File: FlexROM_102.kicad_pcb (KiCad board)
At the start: 2 copper layers, 16.5 x 34.3 mm, 7 parts, among them J1 27C256 DIP LEGS, U1 28C256

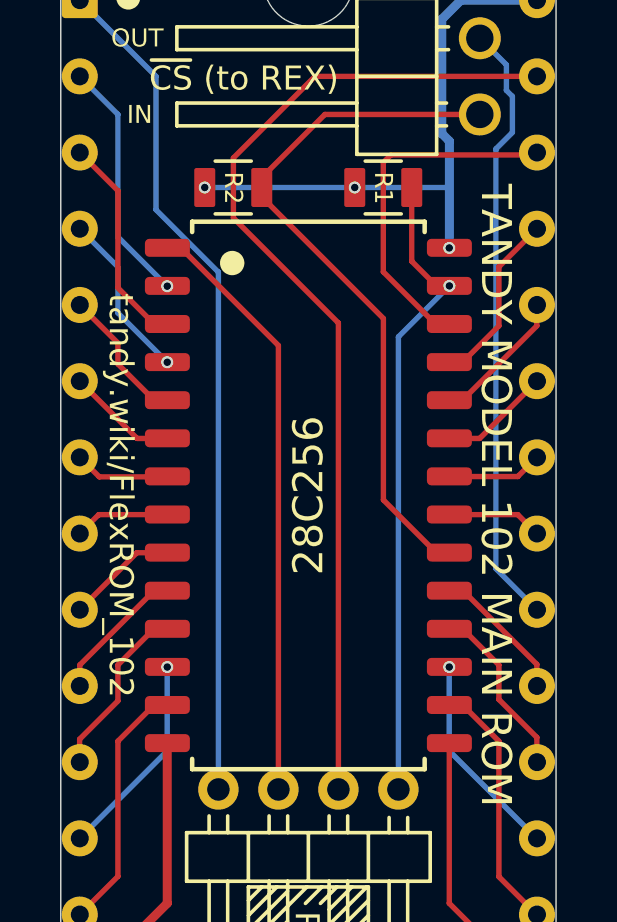
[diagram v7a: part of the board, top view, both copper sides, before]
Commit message: add FlashROM_100_tsop
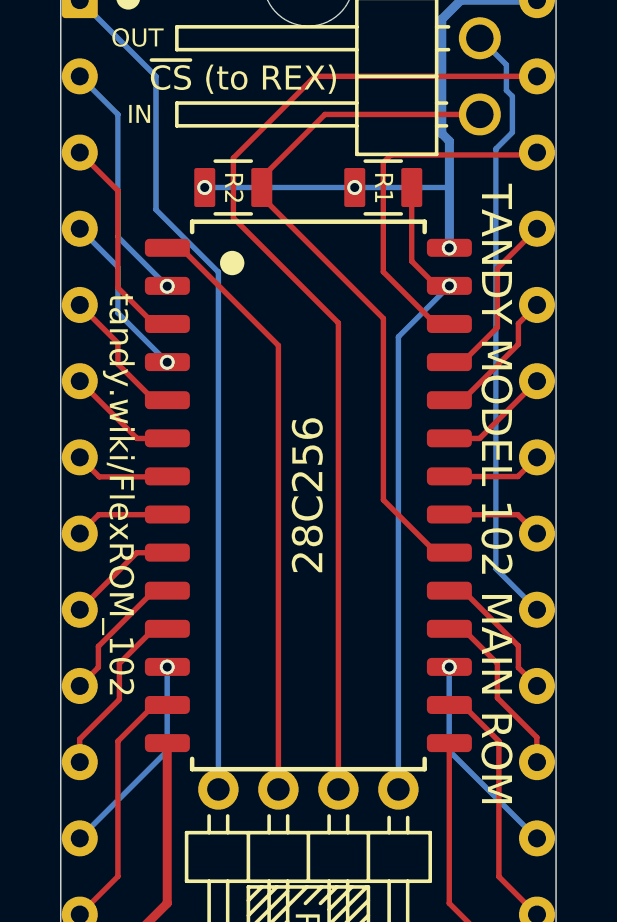
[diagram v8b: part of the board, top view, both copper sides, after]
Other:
- net class Default: via_dia 0.4 -> 0.5; via_drill 0.25 -> 0.3
- rule via_min_drill: 0.25 -> 0.3
- rule via_min_size: 0.4 -> 0.5
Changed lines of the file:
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@@
-(kicad_pcb (version 20171130) (host pcbnew 5.1.8-db9833491~88~ubuntu20.10.1)
+(kicad_pcb (version 20171130) (host pcbnew 5.1.9-73d0e3b20d~88~ubuntu20.10.1)
   (general
     (thickness 1.6)
     (drawings 59)
-    (tracks 134)
+    (tracks 137)
     (zones 0)
     (modules 7)
@@
     (zone_45_only no)
     (trace_min 0.16)
-    (via_size 0.4)
-    (via_drill 0.25)
-    (via_min_size 0.4)
-    (via_min_drill 0.25)
-    (uvia_size 0.4)
-    (uvia_drill 0.25)
+    (via_size 0.5)
+    (via_drill 0.3)
+    (via_min_size 0.5)
+    (via_min_drill 0.3)
+    (uvia_size 0.5)
+    (uvia_drill 0.3)
     (uvias_allowed no)
-    (uvia_min_size 0.4)
-    (uvia_min_drill 0.25)
+    (uvia_min_size 0.5)
+    (uvia_min_drill 0.3)
     (edge_width 0.05)
     (segment_width 0.2)
@@
     (pad_drill 2)
     (pad_to_mask_clearance 0)
+    (solder_mask_min_width 0.22)
     (aux_axis_origin 0 0)
     (grid_origin 127 101.6)
@@
     (clearance 0.16)
     (trace_width 0.18)
-    (via_dia 0.4)
-    (via_drill 0.25)
-    (uvia_dia 0.4)
-    (uvia_drill 0.25)
+    (via_dia 0.5)
+    (via_drill 0.3)
+    (uvia_dia 0.5)
+    (uvia_drill 0.3)
     (add_net /A0)
     (add_net /A1)
@@
     (add_net /~OE)
     (add_net /~WE)
-  )
-  (module 000_LOCAL:NPTH_3mm (layer F.Cu)
-    (at 127 84.455)
-    (fp_text reference REF** (at 0 2.54) (layer F.SilkS) hide
-      (effects (font (size 1.27 1.27) (thickness 0.127)))
-    )
-    (fp_text value NPTH_3mm (at 0 -2.54) (layer F.Fab)
-      (effects (font (size 1.27 1.27) (thickness 0.0127)))
-    )
-    (pad "" np_thru_hole circle (at 0 0) (size 3 3) (drill 3) (layers *.Cu *.Mask))
   )
   (module 000_LOCAL:DIP28_0.6_pcb_sil_pins (layer F.Cu)
@@
       (rotate (xyz 0 0 0))
     )
+  )
+  (module 000_LOCAL:NPTH_3mm (layer F.Cu)
+    (at 127 84.455)
+    (fp_text reference REF** (at 0 2.54) (layer F.SilkS) hide
+      (effects (font (size 1.27 1.27) (thickness 0.127)))
+    )
+    (fp_text value NPTH_3mm (at 0 -2.54) (layer F.Fab)
+      (effects (font (size 1.27 1.27) (thickness 0.0127)))
+    )
+    (pad "" np_thru_hole circle (at 0 0) (size 3 3) (drill 3) (layers *.Cu *.Mask))
   )
   (module 000_LOCAL:PinHeader_1x04_P2.00mm_Horizontal (layer F.Cu)
@@
   (segment (start 131.695 115.195) (end 131.695 109.86) (width 0.18) (layer F.Cu) (net 1))
   (segment (start 134.615 118.115) (end 131.695 115.195) (width 0.18) (layer F.Cu) (net 1))
-  (via (at 122.295 94.625) (size 0.4) (drill 0.25) (layers F.Cu B.Cu) (net 2))
+  (via (at 122.295 94.625) (size 0.5) (drill 0.3) (layers F.Cu B.Cu) (net 2))
   (segment (start 120.65 88.9) (end 119.385 87.635) (width 0.18) (layer B.Cu) (net 2))
   (segment (start 120.65 92.98) (end 120.65 88.9) (width 0.18) (layer B.Cu) (net 2))
@@
   (segment (start 122.295 95.89) (end 121.8615 95.89) (width 0.18) (layer F.Cu) (net 4))
   (segment (start 131.695 107.32) (end 131.695 107.32) (width 0.18) (layer F.Cu) (net 5))
-  (via (at 131.695 107.32) (size 0.4) (drill 0.25) (layers F.Cu B.Cu) (net 5))
+  (via (at 131.695 107.32) (size 0.5) (drill 0.3) (layers F.Cu B.Cu) (net 5))
   (segment (start 131.695 110.115) (end 134.615 113.035) (width 0.18) (layer B.Cu) (net 5))
   (segment (start 131.695 107.32) (end 131.695 110.115) (width 0.18) (layer B.Cu) (net 5))
   (segment (start 122.295 97.16) (end 122.295 97.16) (width 0.18) (layer F.Cu) (net 6))
-  (via (at 122.295 97.16) (size 0.4) (drill 0.25) (layers F.Cu B.Cu) (net 6))
+  (via (at 122.295 97.16) (size 0.5) (drill 0.3) (layers F.Cu B.Cu) (net 6))
   (segment (start 120.65 93.98) (end 119.38 92.71) (width 0.18) (layer B.Cu) (net 6))
   (segment (start 120.65 95.515) (end 120.65 93.98) (width 0.18) (layer B.Cu) (net 6))
   (segment (start 122.295 97.16) (end 120.65 95.515) (width 0.18) (layer B.Cu) (net 6))
   (segment (start 132.1485 106.05) (end 131.695 106.05) (width 0.18) (layer F.Cu) (net 7))
-  (segment (start 133.35 107.2515) (end 132.1485 106.05) (width 0.18) (layer F.Cu) (net 7))
-  (segment (start 133.35 108.4) (end 133.35 107.2515) (width 0.18) (layer F.Cu) (net 7))
-  (segment (start 134.615 109.665) (end 133.35 108.4) (width 0.18) (layer F.Cu) (net 7))
+  (segment (start 133.3 107.2015) (end 132.1485 106.05) (width 0.18) (layer F.Cu) (net 7))
+  (segment (start 133.3 108.35) (end 133.3 107.2015) (width 0.18) (layer F.Cu) (net 7))
+  (segment (start 134.615 109.665) (end 133.3 108.35) (width 0.18) (layer F.Cu) (net 7))
   (segment (start 134.615 110.495) (end 134.615 109.665) (width 0.18) (layer F.Cu) (net 7))
   (segment (start 121.8615 98.43) (end 122.295 98.43) (width 0.18) (layer F.Cu) (net 8))
@@
   (segment (start 120.65 96.52) (end 120.65 97.2185) (width 0.18) (layer F.Cu) (net 8))
   (segment (start 119.38 95.25) (end 120.65 96.52) (width 0.18) (layer F.Cu) (net 8))
-  (segment (start 134.615 107.2312) (end 134.615 107.955) (width 0.18) (layer F.Cu) (net 9))
-  (segment (start 132.1638 104.78) (end 134.615 107.2312) (width 0.18) (layer F.Cu) (net 9))
+  (segment (start 134 106.6162) (end 134 107.34) (width 0.18) (layer F.Cu) (net 9))
+  (segment (start 134 107.34) (end 134.615 107.955) (width 0.18) (layer F.Cu) (net 9))
+  (segment (start 132.1638 104.78) (end 134 106.6162) (width 0.18) (layer F.Cu) (net 9))
   (segment (start 131.695 104.78) (end 132.1638 104.78) (width 0.18) (layer F.Cu) (net 9))
   (segment (start 121.29 99.7) (end 122.295 99.7) (width 0.18) (layer F.Cu) (net 10))
@@
   (segment (start 131.695 99.7) (end 132.71 99.7) (width 0.18) (layer F.Cu) (net 17))
   (segment (start 119.38 107.95) (end 119.375 107.955) (width 0.18) (layer F.Cu) (net 18))
-  (segment (start 119.38 107.2515) (end 119.38 107.95) (width 0.18) (layer F.Cu) (net 18))
-  (segment (start 121.8515 104.78) (end 119.38 107.2515) (width 0.18) (layer F.Cu) (net 18))
+  (segment (start 120 107.33) (end 119.38 107.95) (width 0.18) (layer F.Cu) (net 18))
+  (segment (start 120 106.6315) (end 120 107.33) (width 0.18) (layer F.Cu) (net 18))
+  (segment (start 121.8515 104.78) (end 120 106.6315) (width 0.18) (layer F.Cu) (net 18))
   (segment (start 122.295 104.78) (end 121.8515 104.78) (width 0.18) (layer F.Cu) (net 18))
+  (segment (start 134 96.5619) (end 132.1319 98.43) (width 0.18) (layer F.Cu) (net 19))
   (segment (start 132.1319 98.43) (end 131.695 98.43) (width 0.18) (layer F.Cu) (net 19))
-  (segment (start 134.615 95.9469) (end 132.1319 98.43) (width 0.18) (layer F.Cu) (net 19))
-  (segment (start 134.615 95.255) (end 134.615 95.9469) (width 0.18) (layer F.Cu) (net 19))
+  (segment (start 134 95.87) (end 134 96.5619) (width 0.18) (layer F.Cu) (net 19))
+  (segment (start 134.615 95.255) (end 134 95.87) (width 0.18) (layer F.Cu) (net 19))
   (segment (start 122.295 106.05) (end 122.295 106.05) (width 0.18) (layer F.Cu) (net 20))
   (segment (start 119.375 109.725) (end 119.375 110.495) (width 0.18) (layer F.Cu) (net 20))
-  (segment (start 120.65 108.45) (end 119.375 109.725) (width 0.18) (layer F.Cu) (net 20))
-  (segment (start 120.65 107.25) (end 120.65 108.45) (width 0.18) (layer F.Cu) (net 20))
-  (segment (start 121.85 106.05) (end 120.65 107.25) (width 0.18) (layer F.Cu) (net 20))
+  (segment (start 120.7 107.2) (end 120.7 108.4) (width 0.18) (layer F.Cu) (net 20))
+  (segment (start 121.85 106.05) (end 120.7 107.2) (width 0.18) (layer F.Cu) (net 20))
+  (segment (start 120.7 108.4) (end 119.375 109.725) (width 0.18) (layer F.Cu) (net 20))
   (segment (start 122.295 106.05) (end 121.85 106.05) (width 0.18) (layer F.Cu) (net 20))
-  (segment (start 133.35 93.98) (end 134.615 92.715) (width 0.18) (layer F.Cu) (net 21))
-  (segment (start 133.35 95.9485) (end 133.35 93.98) (width 0.18) (layer F.Cu) (net 21))
-  (segment (start 132.1385 97.16) (end 133.35 95.9485) (width 0.18) (layer F.Cu) (net 21))
+  (segment (start 133.3 94.03) (end 134.615 92.715) (width 0.18) (layer F.Cu) (net 21))
+  (segment (start 133.3 95.9985) (end 133.3 94.03) (width 0.18) (layer F.Cu) (net 21))
+  (segment (start 132.1385 97.16) (end 133.3 95.9985) (width 0.18) (layer F.Cu) (net 21))
   (segment (start 131.695 97.16) (end 132.1385 97.16) (width 0.18) (layer F.Cu) (net 21))
   (segment (start 122.295 107.32) (end 122.295 107.32) (width 0.18) (layer F.Cu) (net 22))
-  (via (at 122.295 107.32) (size 0.4) (drill 0.25) (layers F.Cu B.Cu) (net 22))
+  (via (at 122.295 107.32) (size 0.5) (drill 0.3) (layers F.Cu B.Cu) (net 22))
   (segment (start 122.295 110.115) (end 122.295 107.32) (width 0.18) (layer B.Cu) (net 22))
   (segment (start 119.375 113.035) (end 122.295 110.115) (width 0.18) (layer B.Cu) (net 22))
@@
   (segment (start 122.295 115.195) (end 122.295 109.86) (width 0.3) (layer F.Cu) (net 26))
   (segment (start 119.375 118.115) (end 122.295 115.195) (width 0.3) (layer F.Cu) (net 26))
-  (via (at 131.695 93.35) (size 0.4) (drill 0.25) (layers F.Cu B.Cu) (net 27))
-  (via (at 123.545 91.335) (size 0.4) (drill 0.25) (layers F.Cu B.Cu) (net 27))
-  (via (at 128.545 91.335) (size 0.4) (drill 0.25) (layers F.Cu B.Cu) (net 27))
+  (via (at 131.695 93.35) (size 0.5) (drill 0.3) (layers F.Cu B.Cu) (net 27))
+  (via (at 123.545 91.335) (size 0.5) (drill 0.3) (layers F.Cu B.Cu) (net 27))
+  (via (at 128.545 91.335) (size 0.5) (drill 0.3) (layers F.Cu B.Cu) (net 27))
   (segment (start 128.545 91.335) (end 123.545 91.335) (width 0.18) (layer B.Cu) (net 27))
   (segment (start 134.615 85.095) (end 134.62 85.09) (width 0.3) (layer B.Cu) (net 27))
@@
   (segment (start 130.445 91.335) (end 130.445 91.335) (width 0.18) (layer F.Cu) (net 29))
   (segment (start 131.7 94.615) (end 131.695 94.62) (width 0.18) (layer F.Cu) (net 29))
-  (via (at 131.7 94.615) (size 0.4) (drill 0.25) (layers F.Cu B.Cu) (net 29))
+  (via (at 131.7 94.615) (size 0.5) (drill 0.3) (layers F.Cu B.Cu) (net 29))
   (segment (start 130 96.315) (end 131.7 94.615) (width 0.18) (layer B.Cu) (net 29))
   (segment (start 130 111.4) (end 130 96.315) (width 0.18) (layer B.Cu) (net 29))
